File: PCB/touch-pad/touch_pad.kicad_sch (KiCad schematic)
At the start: 4 parts

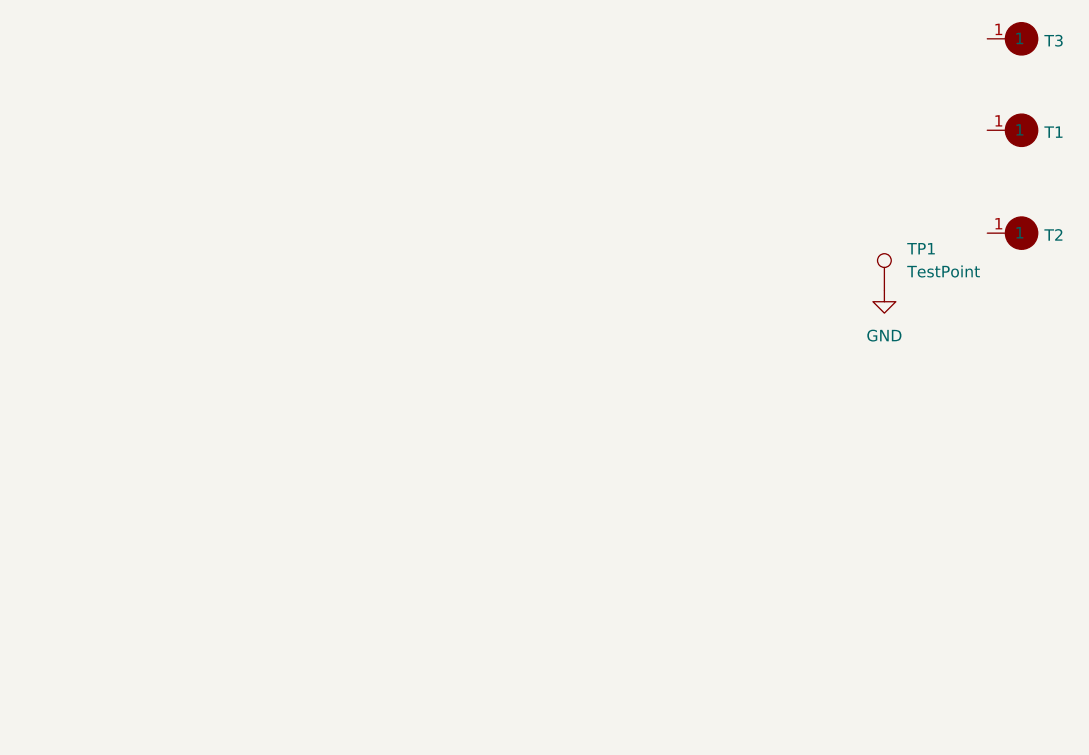
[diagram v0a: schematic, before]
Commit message: Import v2.0 development state from Bitbucket branch v2.0
Overlay of the v2.0 design work onto the restructured PCB/ layout:
- airgradient-go-main v2.0 WIP: 186 footprints, microSD, PS1-CO,
  Birdy schematic review fixes; adds v2.0 BOM CSVs
- touch-pad v2.0: T1-T3 pads wired to touch controller CS channels,
  +3.1V rail renamed to VCC
- scd4x-module: minor updates
- libraries: new parts (SPL07-003, BM05B-SRSS-TB, PS1-CO, battery
  holder, ESP32-C5 models) and updated footprints; all library and
  3D model references normalized to ${KIPRJMOD}-relative paths
- led_pcb board was dropped in v2.0 (never migrated)

Known open items carried over from review: U14 VDD_IO not yet
connected to the 3.1V rail; U19 (LM66200) still fitted.
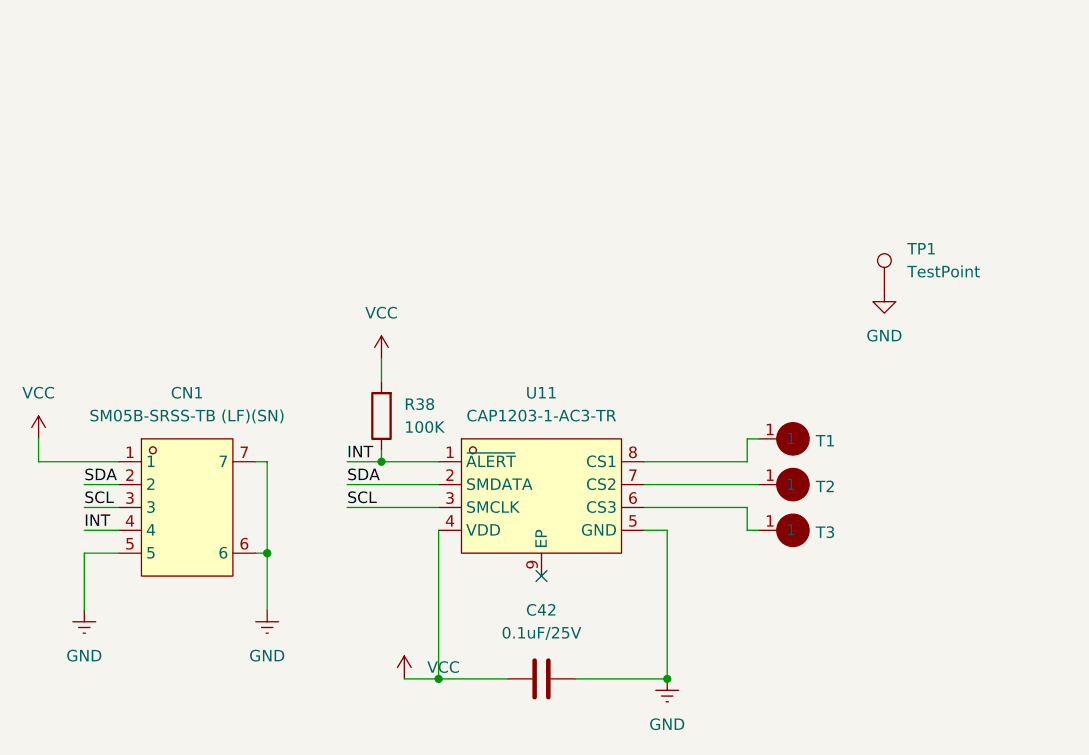
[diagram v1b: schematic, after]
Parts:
- added C42: 0.1uF/25V, Capacitor_SMD:C_0402_1005Metric, symbol Device:C
- added CN1: SM05B-SRSS-TB (LF)(SN), easyeda2kicad-oaf:CONN-SMD_SM05B-SRSS-TB-LF-SN, symbol easyeda2kicad-oaf:SM05B-SRSS-TB(LF)(SN)
- added R38: 100K, Resistor_SMD:R_0402_1005Metric, symbol Device:R
- added U11: CAP1203-1-AC3-TR, easyeda2kicad-oaf:TDFN-8_L3.0-W2.0-P0.50-BL-EP, symbol easyeda2kicad-oaf:CAP1203-1-AC3-TR
- T1, T2, T3: value ~ -> (none); footprint Library:tourch_pad -> Library-oaf:tourch_pad; symbol Library:touch-pad -> Library-oaf:touch-pad
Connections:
- net GND: now also C42.1, CN1.5, CN1.6, CN1.7, U11.5 (GND)
- net at T2.1: now also U11.7 (CS2)
- net at T1.1: now also U11.8 (CS1)
- net at T3.1: now also U11.6 (CS3)
- new net INT: CN1.4, R38.1, U11.1 (~{ALERT})
- new net SCL: CN1.3, U11.3 (SMCLK)
- new net SDA: CN1.2, U11.2 (SMDATA)
- new net VCC: C42.2, CN1.1, R38.2, U11.4 (VDD)
- no-connect marks 0 -> 1
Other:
- moved on the sheet: T1, T2, T3

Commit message: Create production files; switch touch pad connector to Hong Cheng
Mainboard:
- Export v2.0 production files (gerbers, BOM, positions) and 3D STEP model
- Add BOM.csv export

Touch pad:
- Change CN1 connector manufacturer from JST to Hong Cheng HCZZ0032-5 (same housing)
- Regenerate production files as v2.0 (BOM now includes full parts list)
- Add Hong Cheng connector symbol, footprint, and 3D model to easyeda2kicad library
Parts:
- removed CN1: SM05B-SRSS-TB (LF)(SN), easyeda2kicad-oaf:CONN-SMD_SM05B-SRSS-TB-LF-SN, symbol easyeda2kicad-oaf:SM05B-SRSS-TB(LF)(SN)
- added CN1: HCZZ0032-5, easyeda2kicad-oaf:CONN-SMD_HCZZ0032-5, symbol easyeda2kicad-oaf:HCZZ0032-5
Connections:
- net GND: now also U11.9 (EP), CN1.5, CN1.6, CN1.7
- net INT: now also CN1.4
- net SCL: now also CN1.3
- net SDA: now also CN1.2
- net VCC: now also CN1.1
- no-connect marks 1 -> 0
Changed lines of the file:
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@@
 	)
 	(junction
-		(at 107.95 125.73)
+		(at 152.4 129.54)
 		(diameter 0)
 		(color 0 0 0 0)
@@
 	)
 	(junction
+		(at 107.95 132.08)
+		(diameter 0)
+		(color 0 0 0 0)
+	)
+	(junction
 		(at 120.65 115.57)
 		(diameter 0)
 		(color 0 0 0 0)
 	)
-	(no_connect
-		(at 138.43 128.27)
-	)
-	(wire
-		(pts
-			(xy 107.95 132.08) (xy 107.95 125.73)
-		)
-		(stroke
-			(width 0)
-			(type default)
-		)
-	)
 	(wire
 		(pts
@@
 	(wire
 		(pts
+			(xy 152.4 129.54) (xy 152.4 123.19)
+		)
+		(stroke
+			(width 0)
+			(type default)
+		)
+	)
+	(wire
+		(pts
 			(xy 161.29 123.19) (xy 161.29 120.65)
 		)
@@
 	(wire
 		(pts
+			(xy 100.33 132.08) (xy 107.95 132.08)
+		)
+		(stroke
+			(width 0)
+			(type default)
+		)
+	)
+	(wire
+		(pts
 			(xy 161.29 120.65) (xy 149.86 120.65)
 		)
@@
 	(wire
 		(pts
-			(xy 106.68 125.73) (xy 107.95 125.73)
+			(xy 100.33 109.22) (xy 100.33 110.49)
+		)
+		(stroke
+			(width 0)
+			(type default)
+		)
+	)
+	(wire
+		(pts
+			(xy 138.43 128.27) (xy 138.43 129.54)
 		)
 		(stroke
@@
 	(wire
 		(pts
-			(xy 107.95 115.57) (xy 106.68 115.57)
-		)
-		(stroke
-			(width 0)
-			(type default)
-		)
-	)
-	(wire
-		(pts
 			(xy 120.65 104.14) (xy 120.65 106.68)
 		)
@@
 	(wire
 		(pts
-			(xy 107.95 125.73) (xy 107.95 115.57)
+			(xy 107.95 109.22) (xy 107.95 132.08)
 		)
 		(stroke
@@
 	(wire
 		(pts
+			(xy 138.43 129.54) (xy 152.4 129.54)
+		)
+		(stroke
+			(width 0)
+			(type default)
+		)
+	)
+	(wire
+		(pts
 			(xy 120.65 115.57) (xy 127 115.57)
 		)
@@
 	(wire
 		(pts
-			(xy 152.4 139.7) (xy 152.4 123.19)
+			(xy 100.33 132.08) (xy 100.33 130.81)
+		)
+		(stroke
+			(width 0)
+			(type default)
+		)
+	)
+	(wire
+		(pts
+			(xy 152.4 139.7) (xy 152.4 129.54)
 		)
 		(stroke
@@
 		(pts
 			(xy 161.29 113.03) (xy 162.56 113.03)
+		)
+		(stroke
+			(width 0)
+			(type default)
+		)
+	)
+	(wire
+		(pts
+			(xy 107.95 109.22) (xy 100.33 109.22)
 		)
 		(stroke
@@
 			)
 			(justify left bottom)
+		)
+	)
+	(symbol
+		(lib_id "easyeda2kicad-oaf:HCZZ0032-5")
+		(at 96.52 120.65 0)
+		(unit 1)
+		(body_style 1)
+		(exclude_from_sim no)
+		(in_bom yes)
+		(on_board yes)
+		(in_pos_files yes)
+		(dnp no)
+		(fields_autoplaced yes)
+		(property "Reference" "CN1"
+			(at 102.87 119.3799 0)
+			(show_name no)
+			(do_not_autoplace no)
+			(effects
+				(font
+					(size 1.27 1.27)
+				)
+				(justify left)
+			)
+		)
+		(property "Value" "HCZZ0032-5"
+			(at 102.87 121.9199 0)
+			(show_name no)
+			(do_not_autoplace no)
+			(effects
+				(font
+					(size 1.27 1.27)
+				)
+				(justify left)
+			)
+		)
+		(property "Footprint" "easyeda2kicad-oaf:CONN-SMD_HCZZ0032-5"
+			(at 96.52 138.43 0)
+			(hide yes)
+			(show_name no)
+			(do_not_autoplace no)
+			(effects
+				(font
+					(size 1.27 1.27)
+				)
+			)
+		)
+		(property "Datasheet" ""
+			(at 96.52 120.65 0)
+			(hide yes)
+			(show_name no)
+			(do_not_autoplace no)
+			(effects
+				(font
+					(size 1.27 1.27)
+				)
+			)
+		)
+		(property "Description" ""
+			(at 96.52 120.65 0)
+			(hide yes)
+			(show_name no)
+			(do_not_autoplace no)
+			(effects
+				(font
+					(size 1.27 1.27)
+				)
+			)
+		)
+		(property "LCSC Part" "C7433426"
+			(at 96.52 140.97 0)
+			(hide yes)
+			(show_name no)
+			(do_not_autoplace no)
+			(effects
+				(font
+					(size 1.27 1.27)
+				)
+			)
+		)
+		(pin "2"
+		)
+		(pin "3"
+		)
+		(pin "4"
+		)
+		(pin "5"
+		)
+		(pin "6"
+		)
+		(pin "7"
+		)
+		(pin "1"
+		)
+		(instances
+			(project "touch_pad"
+				(path "/6a5d421d-93bc-45c1-8843-32dac20a46e1"
+					(reference "CN1")
+					(unit 1)
+				)
+			)
 		)
 	)
@@
 					(unit 1)
 				)
-			)
-		)
-	)
-	(symbol
-		(lib_id "easyeda2kicad-oaf:SM05B-SRSS-TB(LF)(SN)")
-		(at 99.06 120.65 0)
-		(unit 1)
-		(body_style 1)
-		(exclude_from_sim no)
-		(in_bom yes)
-		(on_board yes)
-		(in_pos_files yes)
-		(dnp no)
-		(fields_autoplaced yes)
-		(property "Reference" "CN1"
-			(at 99.06 107.95 0)
-			(show_name no)
-			(do_not_autoplace no)
-			(effects
-				(font
-					(size 1.27 1.27)
-				)
-			)
-		)
-		(property "Value" "SM05B-SRSS-TB (LF)(SN)"
-			(at 99.06 110.49 0)
-			(show_name no)
-			(do_not_autoplace no)
-			(effects
-				(font
-					(size 1.27 1.27)
-				)
-			)
-		)
-		(property "Footprint" "easyeda2kicad-oaf:CONN-SMD_SM05B-SRSS-TB-LF-SN"
-			(at 99.06 133.35 0)
-			(hide yes)
-			(show_name no)
-			(do_not_autoplace no)
-			(effects
-				(font
-					(size 1.27 1.27)
-				)
-			)
-		)
-		(property "Datasheet" "https://lcsc.com/product-detail/Connectors_JST_SM05B-SRSS-TB-LF-SN_SM05B-SRSS-TB-LF-SN_C136657.html"
-			(at 99.06 135.89 0)
-			(hide yes)
-			(show_name no)
-			(do_not_autoplace no)
-			(effects
-				(font
-					(size 1.27 1.27)
-				)
-			)
-		)
-		(property "Description" ""
-			(at 99.06 120.65 0)
-			(hide yes)
-			(show_name no)
-			(do_not_autoplace no)
-			(effects
-				(font
-					(size 1.27 1.27)
-				)
-			)
-		)
-		(property "LCSC Part" "C136657"
-			(at 99.06 138.43 0)
-			(hide yes)
-			(show_name no)
-			(do_not_autoplace no)
-			(effects
-				(font
-					(size 1.27 1.27)
-				)
-			)
-		)
-		(pin "6"
-		)
-		(pin "7"
-		)
-		(pin "2"
-		)
-		(pin "3"
-		)
-		(pin "1"
-		)
-		(pin "4"
-		)
-		(pin "5"
-		)
-		(instances
-			(project "touch_pad"
-				(path "/6a5d421d-93bc-45c1-8843-32dac20a46e1"
-					(reference "CN1")
-					(unit 1)
-				)
